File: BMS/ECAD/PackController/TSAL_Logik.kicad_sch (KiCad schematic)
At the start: 5 parts, among them Q14 FDN352AP, Q5 BC846

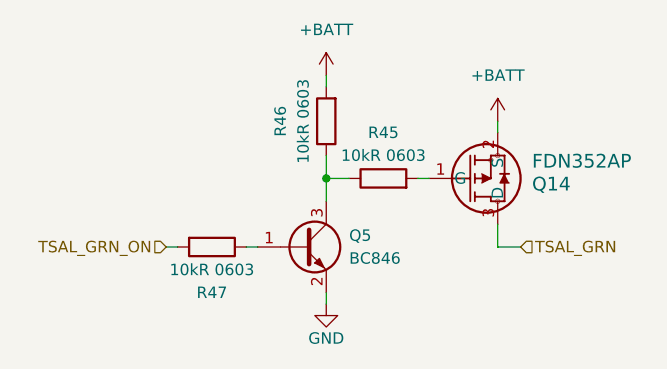
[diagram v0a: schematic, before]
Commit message: close to finish BMS master, only some footprints needed
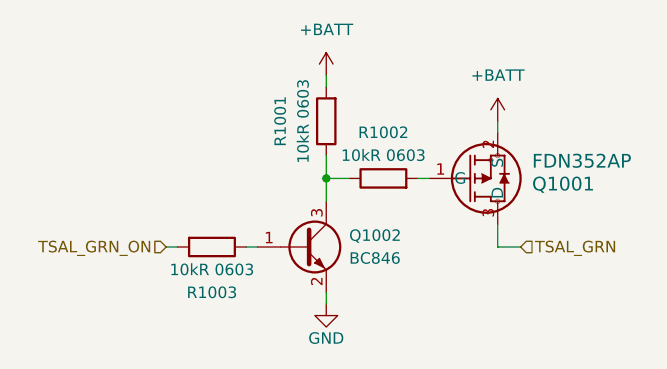
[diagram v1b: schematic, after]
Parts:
- renumbered Q14 to Q1001, Q5 to Q1002, R46 to R1001, R45 to R1002, R47 to R1003

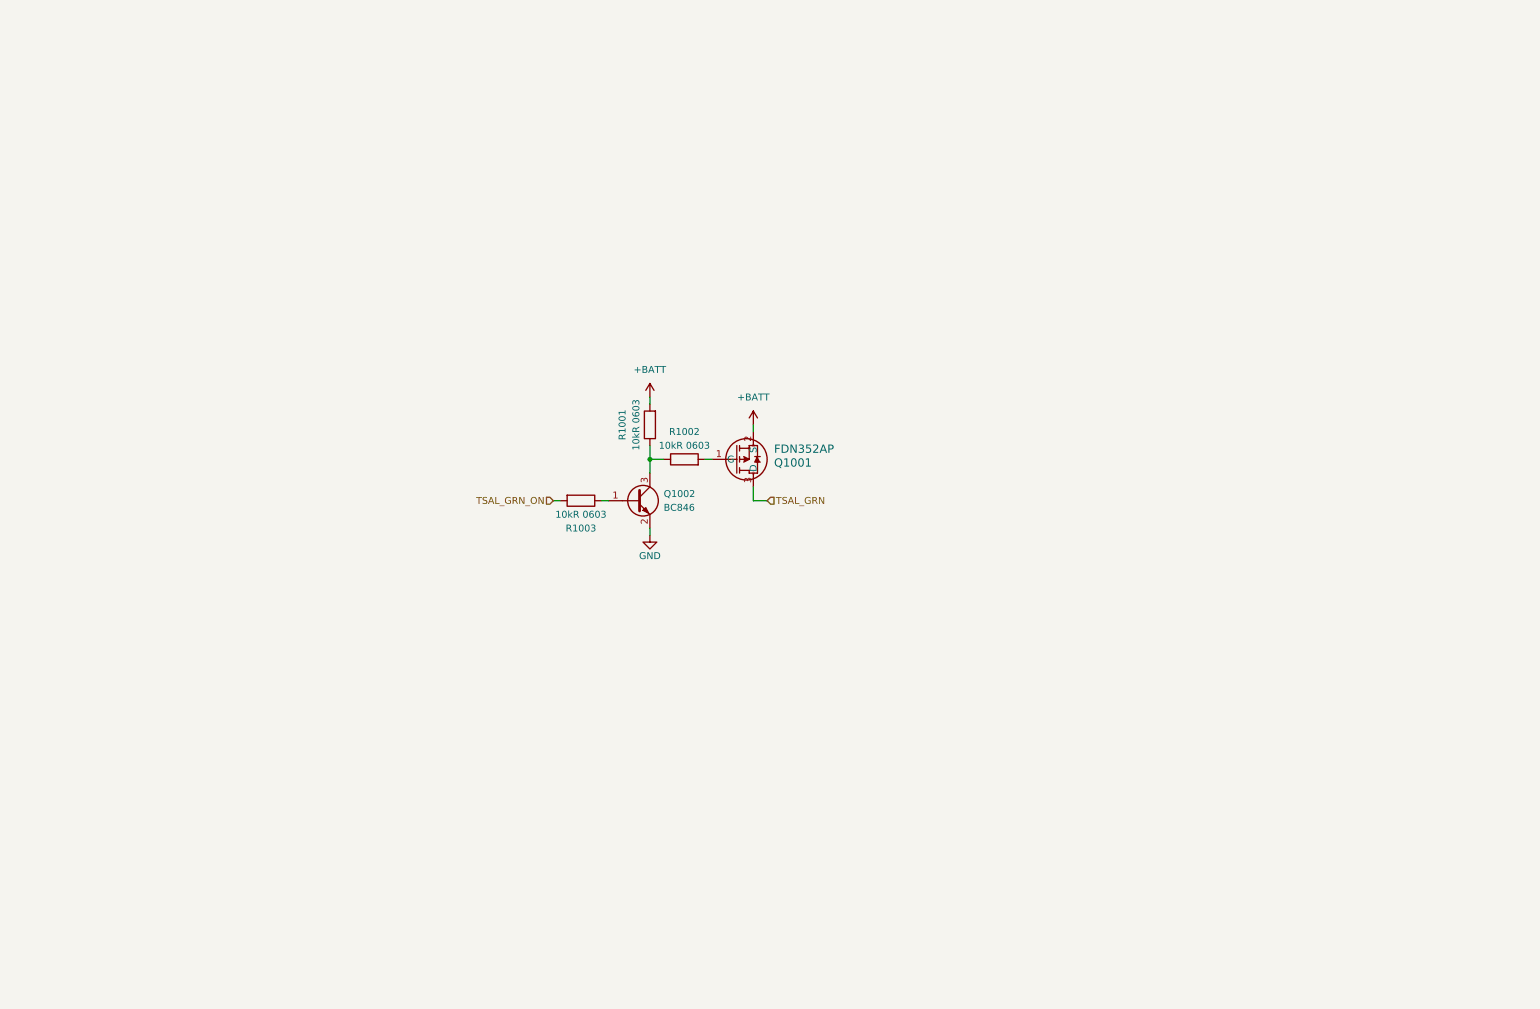
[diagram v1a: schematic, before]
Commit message: Add several auxilary circuits to BMS Master
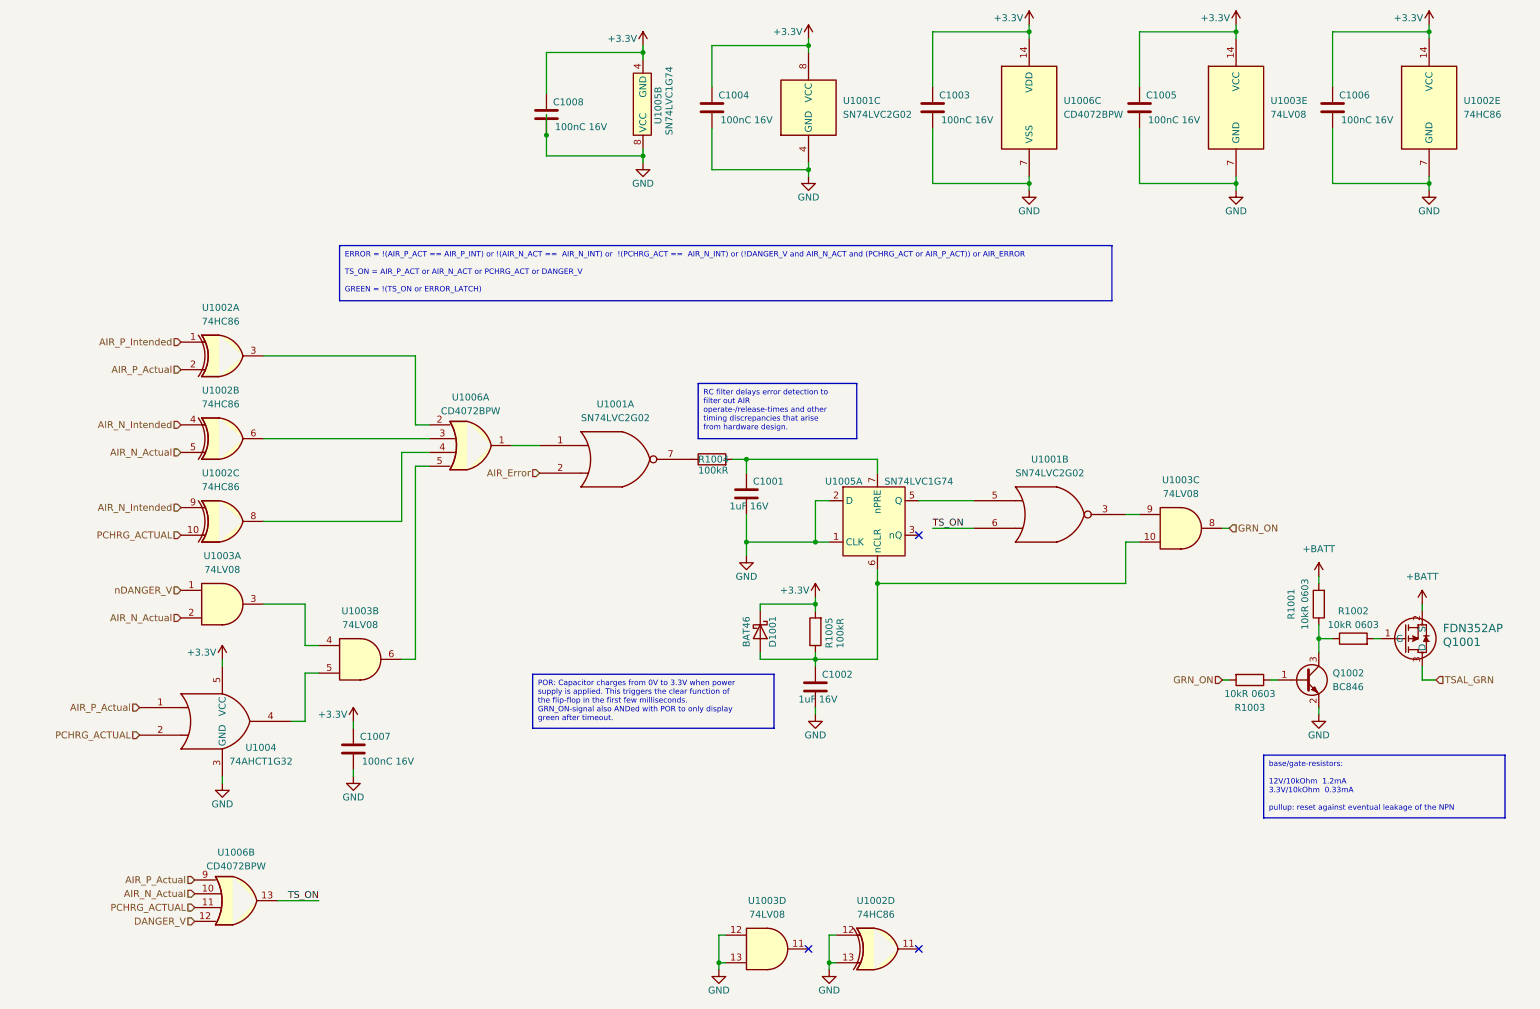
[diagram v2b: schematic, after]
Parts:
- added C1001, C1002: 1uF 16V, Capacitor_SMD:C_0603_1608Metric, symbol Device:C
- added C1003, C1004, C1005, C1006, C1007, C1008: 100nC 16V, Capacitor_SMD:C_0603_1608Metric, symbol Device:C
- added D1001: BAT46, Diode_SMD:D_SOD-123, symbol Diode:BAT46
- added R1004, R1005: 100kR, Resistor_SMD:R_0603_1608Metric, symbol Device:R
- added U1001: SN74LVC2G02, Package_SO:VSSOP-8_2.3x2mm_P0.5mm, symbol 74xGxx:74AUC2G02
- added U1002: 74HC86, Package_SO:SO-14_3.9x8.65mm_P1.27mm, symbol 74xx:74HC86
- added U1003: 74LV08, Package_SO:SO-14_3.9x8.65mm_P1.27mm, symbol 74xx:74LS08
- added U1004: 74AHCT1G32, Package_TO_SOT_SMD:SOT-353_SC-70-5, symbol 74xGxx:74AHCT1G32
- added U1005: SN74LVC1G74, Package_SO:VSSOP-8_2.3x2mm_P0.5mm, symbol EKartParts:SN74LVC1G74
- added U1006: CD4072BPW, Package_SO:TSSOP-14_4.4x5mm_P0.65mm, symbol 4xxx:4072
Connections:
- net GND: now also C1001.2, C1002.2, C1003.2, C1004.2, C1005.2, C1006.2, C1007.2, C1008.2, U1001.4 (GND), U1002.12, U1002.13, U1002.7 (GND), U1003.12, U1003.13, U1003.7 (GND), U1004.3 (GND), U1005.1 (CLK), U1005.2 (D), U1005.8 (VCC), U1006.7 (VSS)
- net TSAL_GRN_ON renamed GRN_ON
- net GRN_ON: now also U1003.8
- new net: C1002.1, D1001.2 (A), R1005.1, U1003.10, U1005.6 (nCLR)
- new net: U1002.6, U1006.3
- new net: U1001.5, U1005.5 (Q)
- new net: C1001.1, R1004.2, U1005.7 (nPRE)
- new net: U1003.3, U1003.4
- new net: U1003.5, U1004.4
- new net: U1003.6, U1006.5
- new net: U1001.3, U1003.9
- new net: U1002.8, U1006.4
- new net: U1001.1, U1006.1
- new net: R1004.1, U1001.7
- new net: U1002.3, U1006.2
- new net +3.3V: C1003.1, C1004.1, C1005.1, C1006.1, C1007.1, C1008.1, D1001.1 (K), R1005.2, U1001.8 (VCC), U1002.14 (VCC), U1003.14 (VCC), U1004.5 (VCC), U1005.4 (GND), U1006.14 (VDD)
- new net AIR_Error: U1001.2
- new net AIR_N_Actual: U1002.5, U1003.2, U1006.10
- new net AIR_N_Intended: U1002.4, U1002.9
- new net AIR_P_Actual: U1002.2, U1004.1, U1006.9
- new net AIR_P_Intended: U1002.1
- new net DANGER_V: U1006.12
- new net PCHRG_ACTUAL: U1002.10, U1004.2, U1006.11
- new net TS_ON: U1001.6, U1006.13
- new net nDANGER_V: U1003.1
- no-connect marks 0 -> 3
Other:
- moved on the sheet: Q1001, Q1002, R1001, R1002, R1003

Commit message: finalised schematic of pack controller
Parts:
- added U1007: SN74LVC2G14DBV, Package_TO_SOT_SMD:SOT-23-6, symbol 74xGxx:SN74LVC2G14DBV
- Q1001: footprint SOT23_527AG_ONS -> Package_TO_SOT_SMD:SOT-23
- U1002: value 74HC86 -> 74LVC86AD
- U1004: value 74AHCT1G32 -> 74LVC1G32Q
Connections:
- net +3.3V: now also U1007.5 (V_{CC})
- net GND: now also U1007.2 (GND)
- net at C1002.1, D1001.2 (A), R1005.1: now also U1007.3 (2A); no longer U1003.10, U1005.6 (nCLR)
- new net: U1003.10, U1005.6 (nCLR), U1007.6 (1Y)
- new net: U1007.1 (1A), U1007.4 (2Y)
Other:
- moved on the sheet: C1002, D1001, R1005

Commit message: many fixes
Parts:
- added D1002, D1003: BAT46, Diode_SMD:D_SOD-123, symbol Diode:BAT46
- added R1006: 1kR, Resistor_SMD:R_0603_1608Metric, symbol Device:R
- added U1008: SN74LVC2G14DBV, Package_TO_SOT_SMD:SOT-23-6, symbol 74xGxx:SN74LVC2G14DBV
- U1007: value SN74LVC2G14DBV -> SN74LVC2G17DCK; symbol 74xGxx:SN74LVC2G14DBV -> EKartParts:SN74LVC2G17
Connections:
- net +3.3V: now also U1008.5 (V_{CC})
- net AIR_Error: now also U1008.6 (1Y)
- net DANGER_V: now also U1008.4 (2Y)
- net GND: now also U1008.2 (GND)
- net TSAL_GRN: now also D1003.1 (K); no longer Q1001.3 (D)
- net nDANGER_V: now also U1008.3 (2A)
- net at U1003.10, U1005.6 (nCLR): now also U1007.4 (2Y); no longer U1007.6 (1Y)
- net at C1001.1, R1004.2: now also U1007.1 (1A), R1006.2; no longer U1005.7 (nPRE)
- net at R1004.1, U1001.7: now also D1002.2 (A)
- new net: U1005.7 (nPRE), U1007.6 (1Y)
- new net: D1003.2 (A), Q1001.3 (D)
- new net: D1002.1 (K), R1006.1
- new net nAIR_Error: U1008.1 (1A)
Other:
- moved on the sheet: C1001, C1002, C1007, D1001, Q1001, Q1002, R1001, R1002, R1003, R1004, R1005, U1001A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

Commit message: add rule areas for hv separation
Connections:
- net AIR_P_Actual: no longer U1004.1
- new net PCHRG_Intended: U1004.1
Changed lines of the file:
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@@
 		)
 	)
-	(text_box "POR: Capacitor charges from 0V to 3.3V when power supply is applied. This triggers the clear function of the flip-flop in the first few milliseconds.\nGRN_ON-signal also ANDed with POR to only display green after timeout."
+	(text_box "POR: Capacitor charges from 0V to 3.3V when power supply is applied. This triggers the clear function of the flip-flop. \nPOR keeps nCLR active for approximately 50...95 ms nominal. \nActual delay depends on Schmitt threshold and RC tolerances.\nGRN_ON-signal also ANDed with POR to only display green after timeout."
 		(exclude_from_sim no)
 		(at 167.64 128.27 0)
-		(size 44.45 9.9536)
+		(size 44.45 16.3934)
 		(margins 0.9525 0.9525 0.9525 0.9525)
 		(stroke
@@
 		)
 	)
+	(hierarchical_label "PCHRG_Intended"
+		(shape input)
+		(at 27.94 143.51 180)
+		(effects
+			(font
+				(size 1.27 1.27)
+			)
+			(justify right)
+		)
+	)
 	(hierarchical_label "AIR_P_Intended"
 		(shape input)
@@
 		(effects
 			(font
-				(size 1.27 1.27)
-			)
-			(justify right)
-		)
-	)
-	(hierarchical_label "AIR_P_Actual"
-		(shape input)
-		(at 27.94 143.51 180)
-		(effects
-			(font

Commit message: yes
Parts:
- C1001, C1002: value 1uF 16V -> 1uF 100V; footprint Capacitor_SMD:C_0603_1608Metric -> Capacitor_SMD:C_0805_2012Metric
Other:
- moved on the sheet: C1001, C1002, C1007, D1001, D1002, D1003, Q1001, Q1002, R1001, R1002, R1003, R1004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
